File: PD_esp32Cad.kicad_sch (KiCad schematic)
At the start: 27 parts, among them J1 USB_C_Receptacle_USB2.0_14P, SW1 reset, SW2 BOOT, U1 ESP32-S3-WROOM-1, U2 LM5148RGYR, U4 AP63203WU, U5 CYPD3177-24LQ

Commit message: PD_sink
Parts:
- added C18, C19: 1u, symbol Device:C
- added Q3, Q4: FDS6975, symbol Simulation_SPICE:PMOS
- added R3: 55k, symbol Device:R
- added R4: 2k2, symbol Device:R
- added R5: 20k, symbol Device:R
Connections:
- net VBUS: now also C18.1, Q3.1 (D), R5.1
- net +20V: now reaches U5.11 (VDC_OUT)
- net +20V: now also C19.1, Q4.1 (D)
- net at U5.3 (VBUS_FET_EN): now also R4.1
- new net: Q3.2 (G), Q4.2 (G), R3.1
- new net: C18.2, C19.2, R3.2, R4.2, R5.2
- new net: Q3.3 (S), Q4.3 (S)
- no-connect marks 4 -> 5
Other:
- note added: "PD Sink"
- moved on the sheet: C11, C12, C13, C14, C15, C16, C17, C7, C8, R2, U5

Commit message: Esp32 progress
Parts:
- added R6: 2k2, symbol Device:R
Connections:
- net +3.3V: now also C2.1, C3.1, R6.1
- net D+: now also U1.14 (USB_D+)
- net D-: now also U1.13 (USB_D-)
- net GND: now also U1.1 (GND), U1.40 (GND), U1.41 (GND)
- net EN: now reaches C1.2, R1.2, SW1.2, U1.3 (EN)
- net BOOT: now reaches C4.2, SW2.2, U1.27 (IO0)
- net BOOT: now also R6.2
- no-connect marks 5 -> 6
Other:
- moved on the sheet: C1, C2, C3, R1, SW1, U1, U2

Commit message: Update PD_esp32Cad.kicad_sch
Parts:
- removed U4: AP63203WU, Package_TO_SOT_SMD:TSOT-23-6, symbol Regulator_Switching:AP63203WU
- added U3: AP63205WU, Package_TO_SOT_SMD:TSOT-23-6, symbol Regulator_Switching:AP63205WU
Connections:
- net +3.3V: no longer C10.2, C9.2, L1.2
- net GND: now also U3.4 (GND)
- net VBUS: now also U3.2 (EN), U3.3 (IN)
- net at C6.2, L1.1: now also U3.6 (BST)
- net at C6.1: now also U3.5 (SW)
- new net +5V: C10.2, C9.2, L1.2, U3.1 (FB)
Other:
- note added: "Vbus to 5V Power Supply"
- note removed: "Esp32 Power Supply"
- moved on the sheet: C10, C5, C6, C9, L1, U2

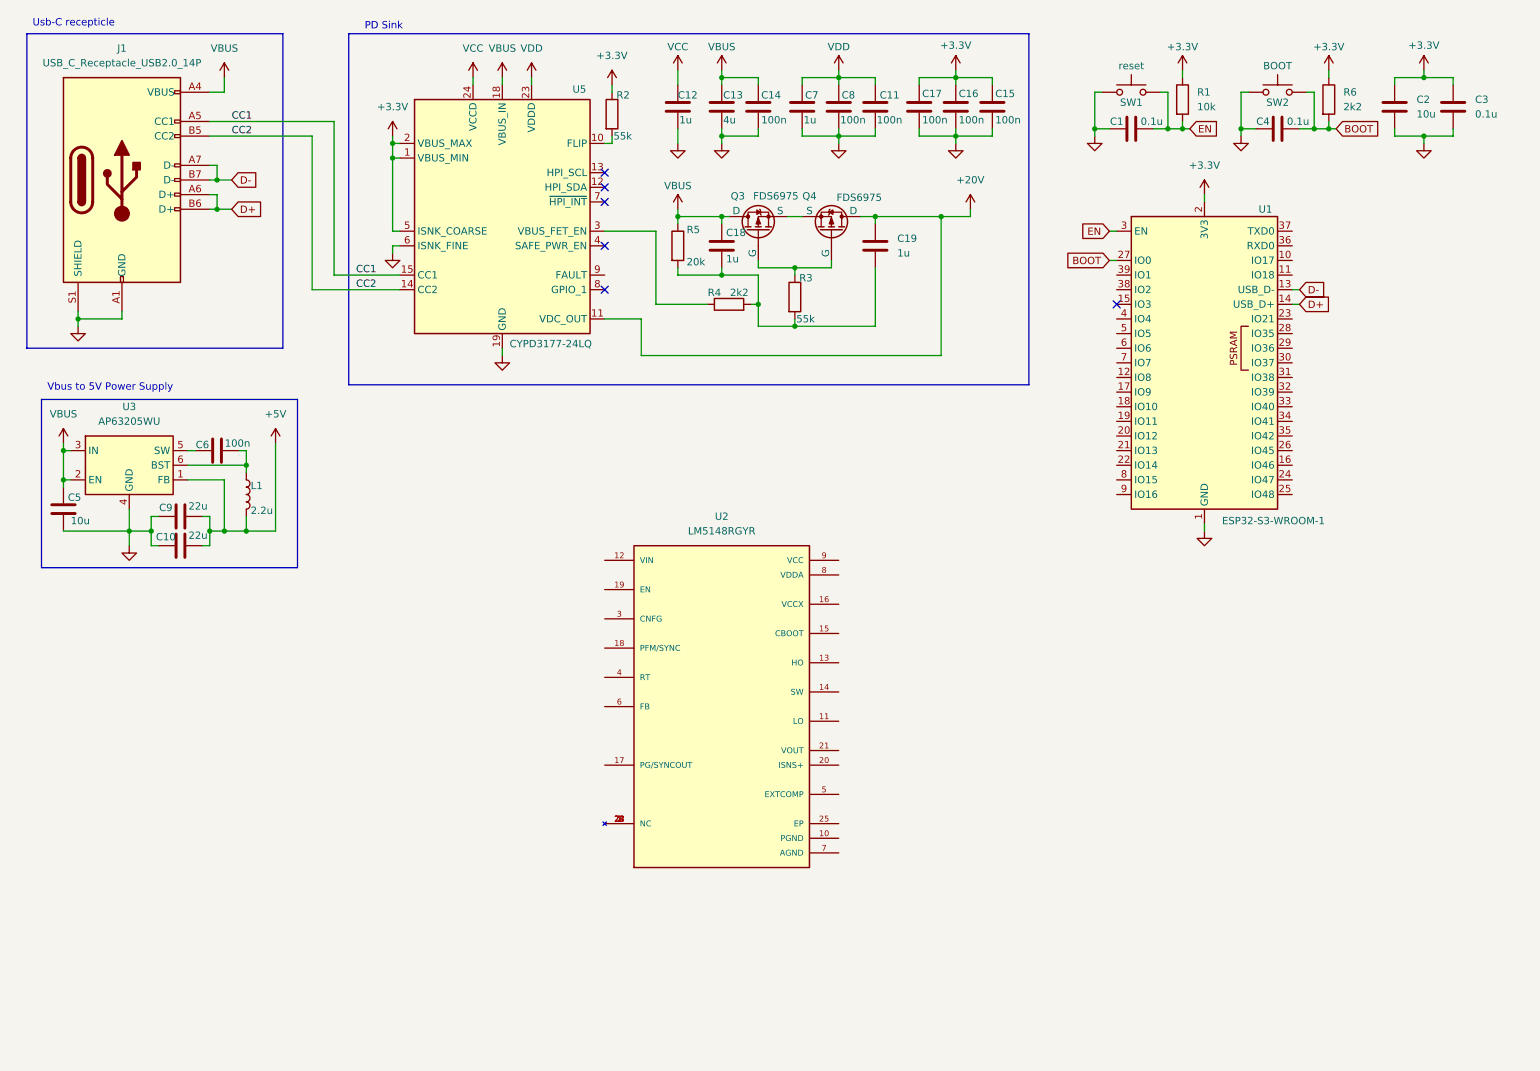
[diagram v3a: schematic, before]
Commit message: update
working on final single output dual phase bucks 20v -> 5v 20A.
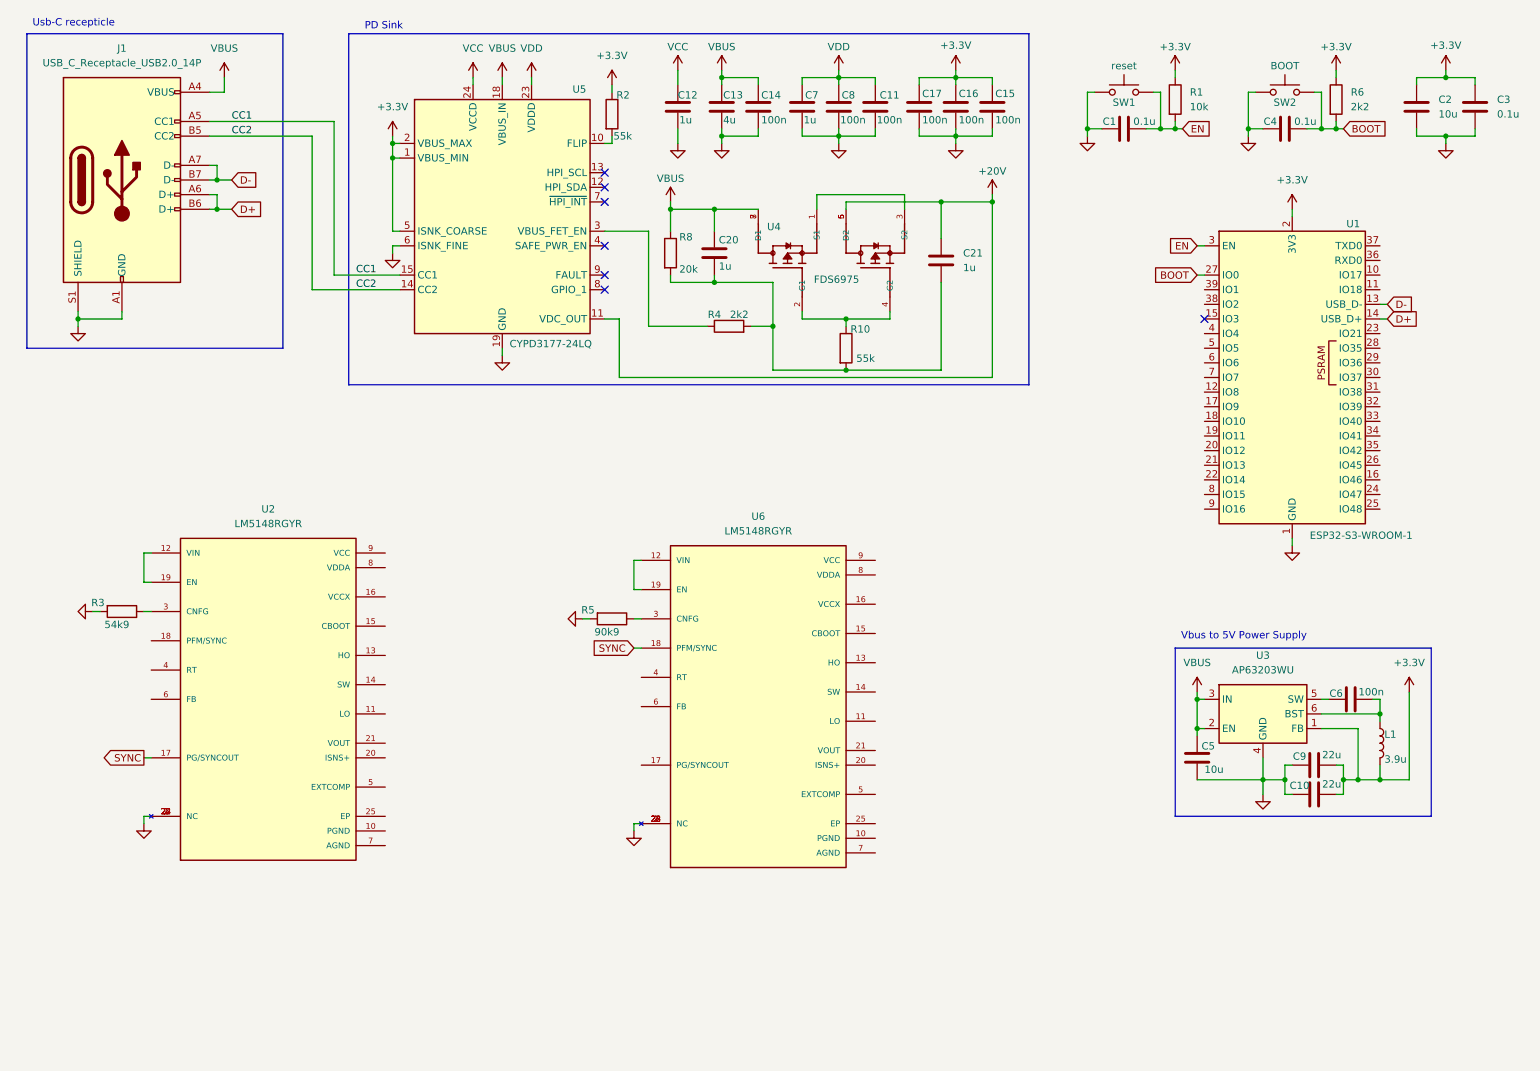
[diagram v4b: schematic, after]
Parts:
- removed C18, C19: 1u, symbol Device:C
- removed Q3, Q4: FDS6975, symbol Simulation_SPICE:PMOS
- removed U3: AP63205WU, Package_TO_SOT_SMD:TSOT-23-6, symbol Regulator_Switching:AP63205WU
- added C20, C21: 1u, symbol Device:C
- added R10: 55k, symbol Device:R
- added R8: 20k, symbol Device:R
- added U3: AP63203WU, Package_TO_SOT_SMD:TSOT-23-6, symbol Regulator_Switching:AP63203WU
- added U4: FDS6975, FDS6975:SOIC127P600X175-8N, symbol FDS6975:FDS6975
- added U6: LM5148RGYR, LM5148RGYR:QFN50P550X350X100-25N, symbol LM5148RGYR:LM5148RGYR
- L1: value 2.2u -> 3.9u
- R3: value 55k -> 54k9
- R5: value 20k -> 90k9
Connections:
- net +5V is gone; now on net +3.3V: C10.2, C9.2, L1.2
- net +20V: now also C21.1, U4.5 (D2), U4.6 (D2)
- net +3.3V: now also U3.1 (FB)
- net GND: now also R3.2, R5.2, U2.1 (NC), U2.2 (NC), U2.22 (NC), U2.23 (NC), U2.24 (NC), U3.4 (GND), U6.1 (NC), U6.2 (NC), U6.22 (NC), U6.23 (NC), U6.24 (NC)
- net VBUS: now also C20.1, R8.1, U3.2 (EN), U3.3 (IN), U4.7 (D1), U4.8 (D1); no longer R5.1
- net at R3.1: now also U2.3 (CNFG)
- net at C6.1: now also U3.5 (SW)
- net at C6.2, L1.1: now also U3.6 (BST)
- net at U2.12 (VIN): now also U2.19 (EN)
- net SYNC: now reaches U2.17 (PG/SYNCOUT)
- net SYNC: now also U6.18 (PFM/SYNC)
- new net: U4.1 (S1), U4.3 (S2)
- new net: R10.1, U4.2 (G1), U4.4 (G2)
- new net: C20.2, C21.2, R10.2, R4.2, R8.2
- new net: R5.1, U6.3 (CNFG)
- new net: U6.12 (VIN), U6.19 (EN)
- no-connect marks 6 -> 7
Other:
- moved on the sheet: C1, C10, C2, C3, C4, C5, C6, C9, L1, R1, R4, R6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

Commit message: update
Dual Phase Buck
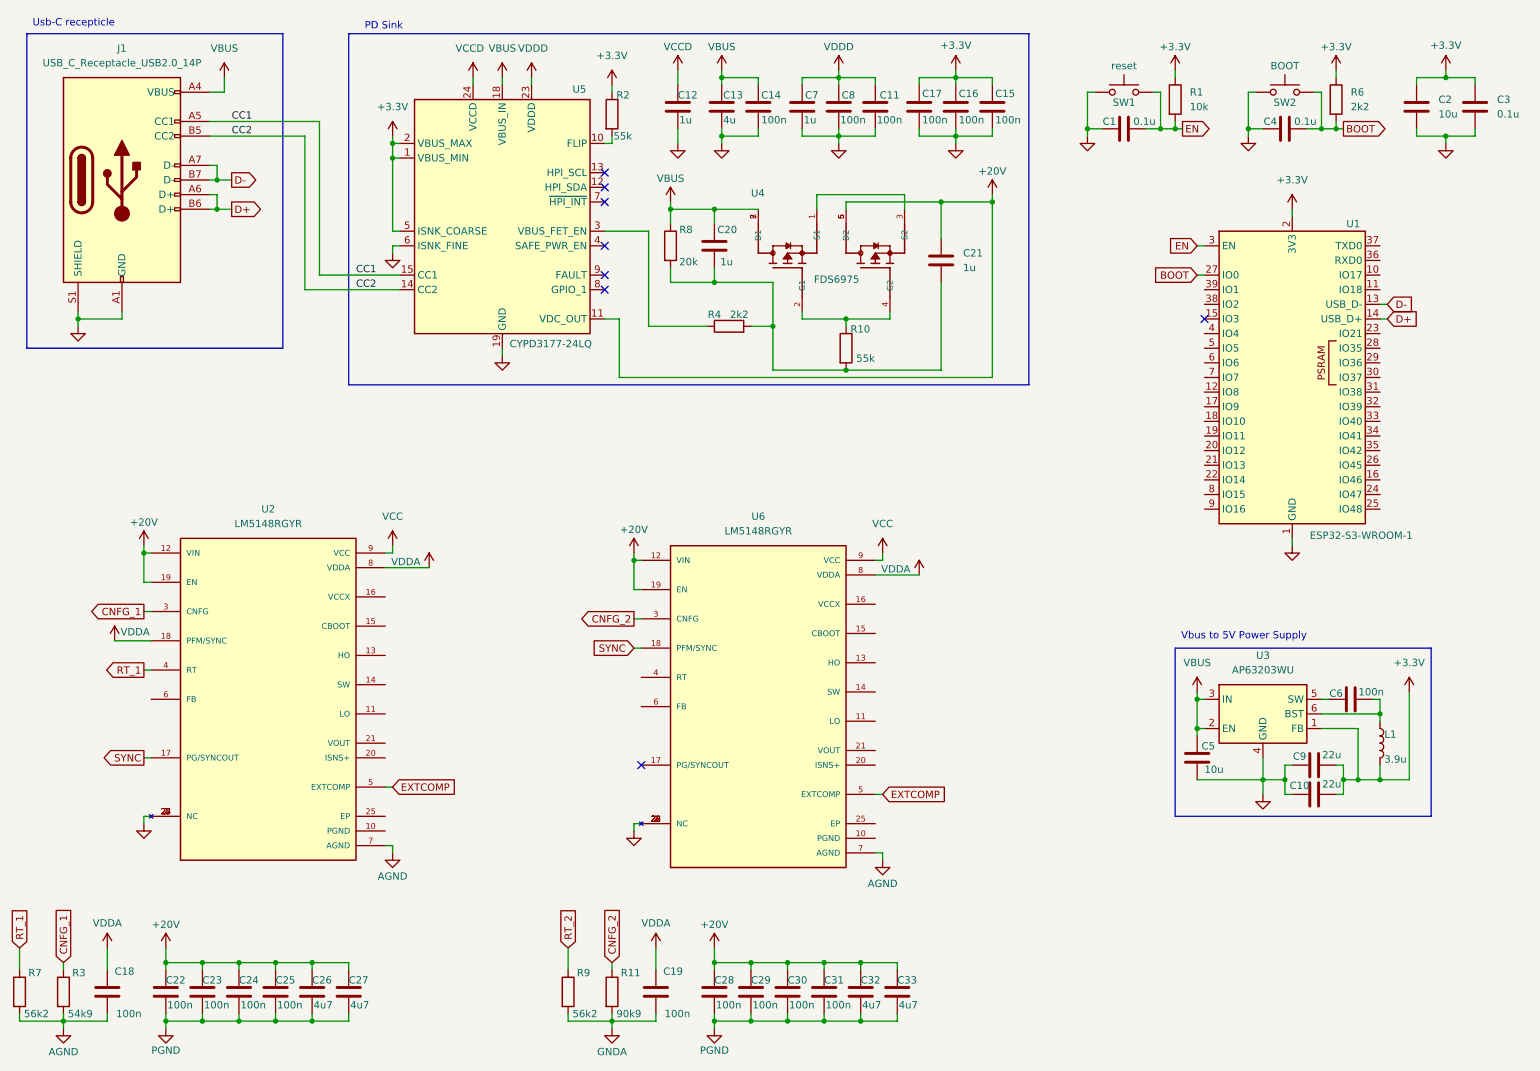
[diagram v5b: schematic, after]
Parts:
- removed R5: 90k9, symbol Device:R
- added C18, C19, C22, C23, C24, C25, C28, C29, C30, C31: 100n, symbol Device:C
- added C26, C27, C32, C33: 4u7, symbol Device:C
- added R11: 90k9, symbol Device:R
- added R7, R9: 56k2, symbol Device:R
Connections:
- net +20V: now also U2.12 (VIN), U2.19 (EN), U6.12 (VIN), U6.19 (EN), C22.1, C23.1, C24.1, C25.1, C26.1, C27.1, C28.1, C29.1, C30.1, C31.1, C32.1, C33.1
- net GND: no longer R3.2
- net VCC: now also U2.9 (VCC), U6.9 (VCC); no longer C12.1, U5.24 (VCCD)
- net CNFG_2: now reaches U6.3 (CNFG)
- net CNFG_2: now also R11.1
- net VDDA: now reaches U2.18 (PFM/SYNC)
- net VDDA: now also U2.8 (VDDA), U6.8 (VDDA), C18.1, C19.1
- net CNFG_1: now reaches R3.1, U2.3 (CNFG)
- net RT_1: now reaches U2.4 (RT)
- net RT_1: now also R7.1
- net EXTCOMP: now reaches U2.5 (EXTCOMP)
- net EXTCOMP: now also U6.5 (EXTCOMP)
- net AGND: now reaches U2.7 (AGND)
- net AGND: now also R3.2, U6.7 (AGND), C18.2, R7.2
- net VDD renamed VDDD
- new net GNDA: C19.2, R11.2, R9.2
- new net PGND: C22.2, C23.2, C24.2, C25.2, C26.2, C27.2, C28.2, C29.2, C30.2, C31.2, C32.2, C33.2
- new net RT_2: R9.1
- new net VCCD: C12.1, U5.24 (VCCD)
- no-connect marks 7 -> 8
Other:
- moved on the sheet: C20, R3, R8

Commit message: update
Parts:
- added C34, C35: ?, symbol Device:C
- added R12: 24k9, symbol Device:R
- added R13: ?, symbol Device:R
- added R5: 130 k, symbol Device:R
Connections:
- net AGND: now also C34.2, C35.2, R12.2
- net EXTCOMP: now also C34.1, R13.1
- net RT_2: now also U6.4 (RT)
- net at U2.6 (FB): now also R12.1, R5.2
- new net: C35.1, R13.2
- new net +5V: R5.1
